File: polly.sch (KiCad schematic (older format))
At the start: 40 parts, among them J5 Conn_02x06_Odd_Even, P1 Power, P2 Analog, P3 Digital, P4 Digital, P5 CONN_01X01, P6 CONN_01X01, P7 CONN_01X01, P8 CONN_01X01, U1 4051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

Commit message: Adjust layout
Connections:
- net +5VA: now also P2.4 (Pin_4); no longer P2.2 (Pin_2)
- net DAC_OUTPUT: now also P2.2 (Pin_2); no longer P2.3 (Pin_3)
- net NOISE: now also P2.3 (Pin_3); no longer P2.4 (Pin_4)
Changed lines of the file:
@@
 	9000 2700 8700 2700
-Wire Wire Line
-	9000 2800 8700 2800
 Wire Wire Line
 	9000 2900 8500 2900
@@
 Text Label 6100 4150 0    50   ~ 0
 LP_CUTOFF
+Text Label 8700 2600 2    50   ~ 0
+DAC_OUTPUT
 Text Label 8700 2700 2    50   ~ 0
-DAC_OUTPUT
-Text Label 8700 2800 2    50   ~ 0
 NOISE
 Text Label 8700 3000 2    50   ~ 0
@@
 L power:+5VA #PWR0104
 U 1 1 6128896C
-P 8700 2600
-F 0 "#PWR0104" H 8700 2450 50  0001 C CNN
-F 1 "+5VA" H 8750 2800 50  0000 C CNN
-F 2 "" H 8700 2600 50  0001 C CNN
-F 3 "" H 8700 2600 50  0001 C CNN
-	1    8700 2600
+P 8550 2800
+F 0 "#PWR0104" H 8550 2650 50  0001 C CNN
+F 1 "+5VA" H 8600 3000 50  0000 C CNN
+F 2 "" H 8550 2800 50  0001 C CNN
+F 3 "" H 8550 2800 50  0001 C CNN
+	1    8550 2800
 	1    0    0    -1
 $EndComp
@@
 PARAM_SEL_A
 NoConn ~ 9800 1500
+Wire Wire Line
+	8550 2800 9000 2800
 $EndSCHEMATC

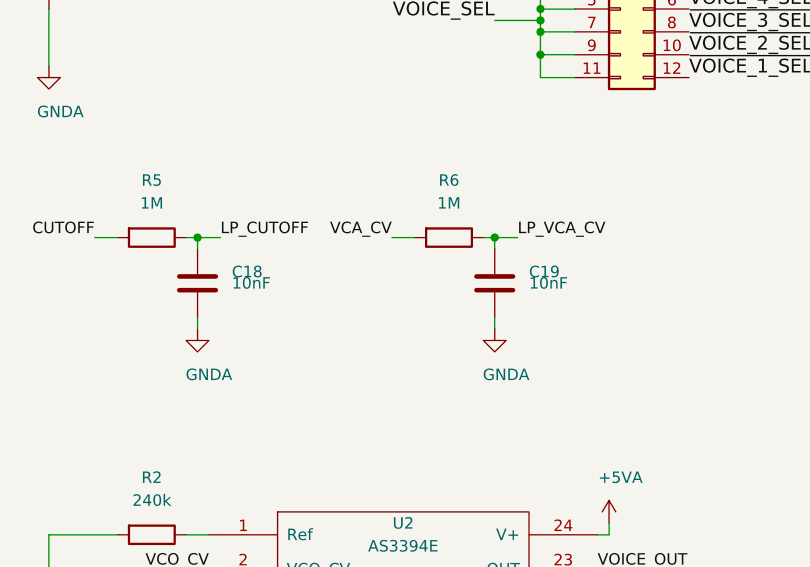
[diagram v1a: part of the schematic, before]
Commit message: Imporove layout for single sided, add previous versions
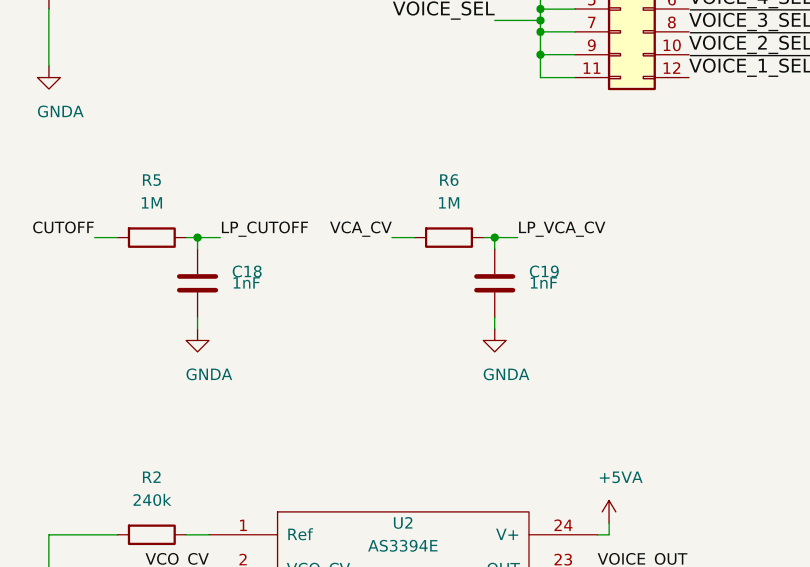
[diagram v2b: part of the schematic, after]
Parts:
- C18, C19: value 10nF -> 1nF
- C8: footprint Capacitor_THT:C_Disc_D3.0mm_W1.6mm_P2.50mm -> Capacitor_THT:C_Rect_L7.2mm_W2.5mm_P5.00mm_FKS2_FKP2_MKS2_MKP2
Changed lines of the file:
@@
 F 0 "C8" H 7950 4850 50  0000 R CNN
 F 1 "560pF" H 7950 4950 50  0000 R CNN
-F 2 "Capacitor_THT:C_Disc_D3.0mm_W1.6mm_P2.50mm" H 8138 4750 50  0001 C CNN
+F 2 "Capacitor_THT:C_Rect_L7.2mm_W2.5mm_P5.00mm_FKS2_FKP2_MKS2_MKP2" H 8138 4750 50  0001 C CNN
 F 3 "~" H 8100 4900 50  0001 C CNN
 	1    8100 4900
@@
 P 5650 2450
 F 0 "C19" H 5800 2500 50  0000 L CNN
-F 1 "10nF" H 5800 2450 50  0000 L CNN
+F 1 "1nF" H 5800 2450 50  0000 L CNN
 F 2 "Capacitor_THT:C_Rect_L7.0mm_W2.0mm_P5.00mm" H 5688 2300 50  0001 C CNN
 F 3 "~" H 5650 2450 50  0001 C CNN
@@
 P 4350 2450
 F 0 "C18" H 4500 2500 50  0000 L CNN
-F 1 "10nF" H 4500 2450 50  0000 L CNN
+F 1 "1nF" H 4500 2450 50  0000 L CNN
 F 2 "Capacitor_THT:C_Rect_L7.0mm_W2.0mm_P5.00mm" H 4388 2300 50  0001 C CNN
 F 3 "~" H 4350 2450 50  0001 C CNN
